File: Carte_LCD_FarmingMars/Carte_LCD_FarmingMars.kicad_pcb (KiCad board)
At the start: 2 copper layers, 17 parts, among them J2 Conn_01x02_Pin, J3 Conn_01x04_Pin, SW1 SW_DIP_x01, SW2 SW_Push, SW3 SW_Push, U1 3V3 reg, U2 ATtiny1616-S

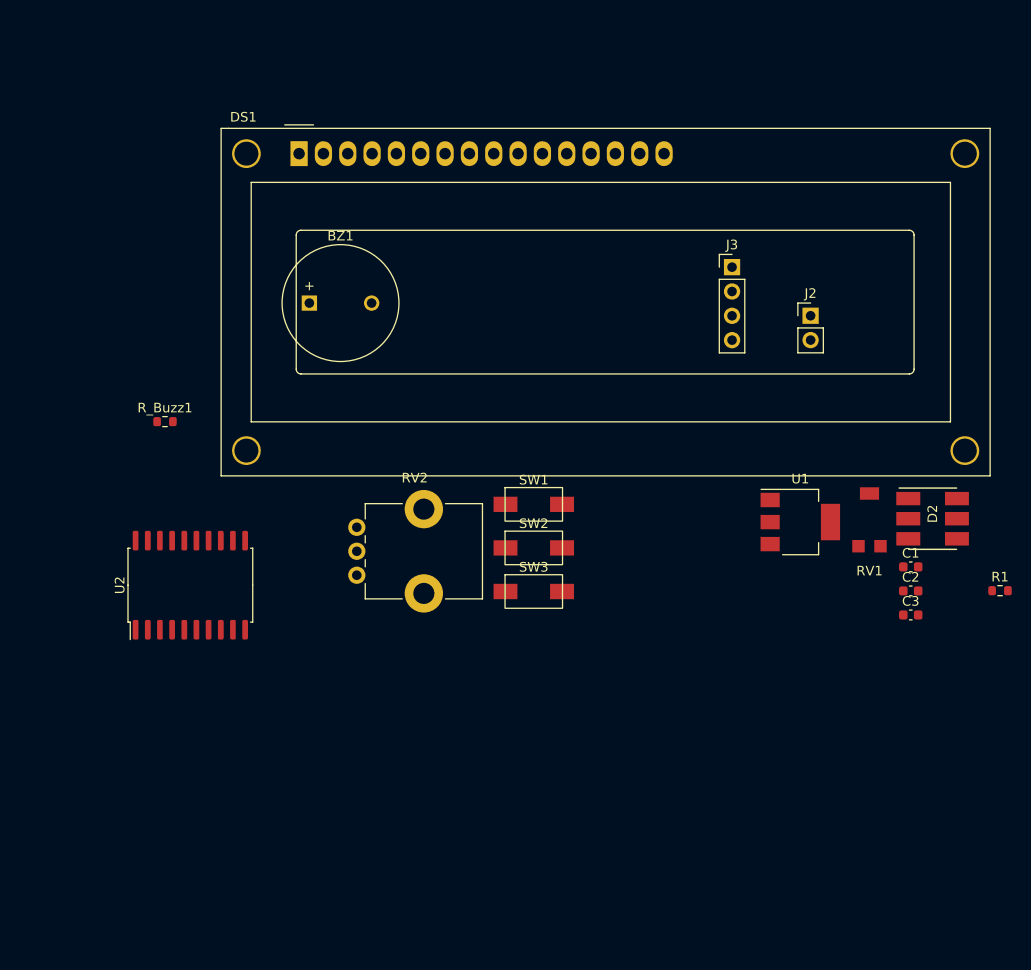
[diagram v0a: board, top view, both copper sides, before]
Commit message: Placement préliminaire PCB
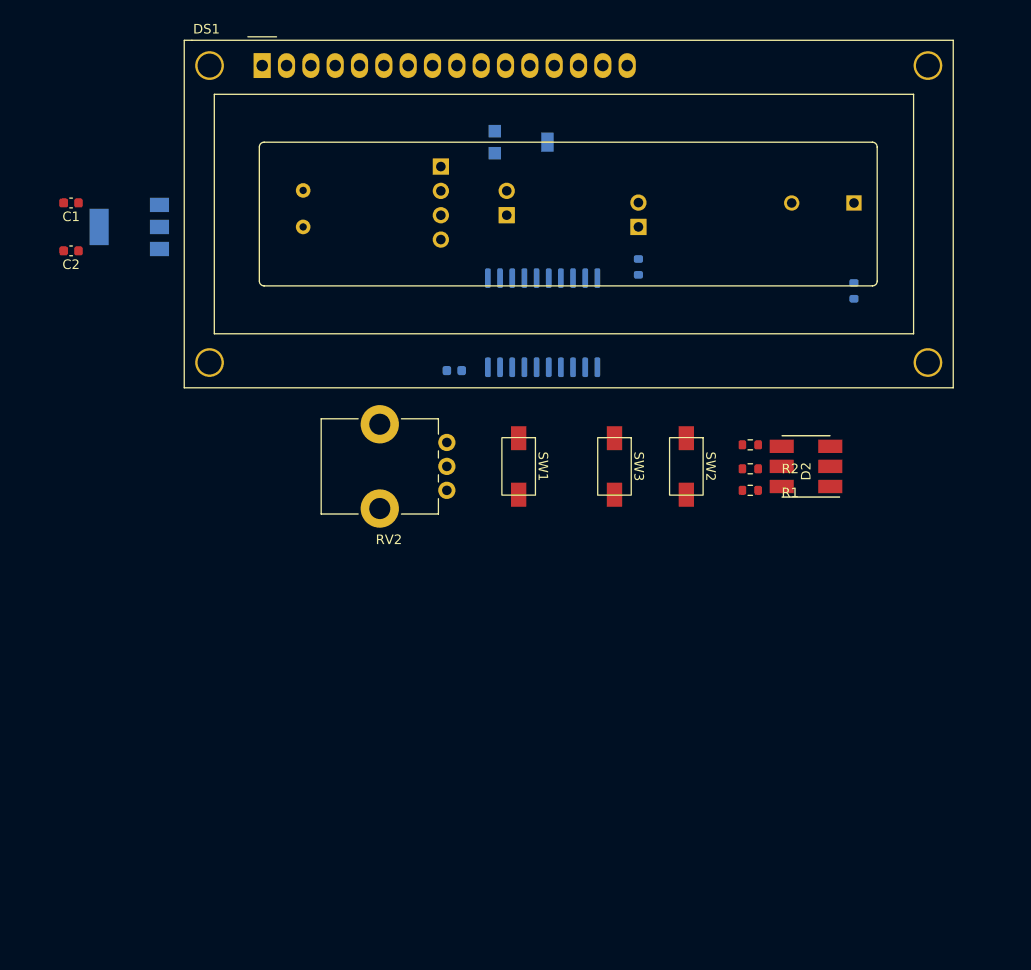
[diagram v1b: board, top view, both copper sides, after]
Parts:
- added J1: Screw_Terminal_01x02, ENAC_robotique:Bornier_2x3.81mm, B.Cu at (107.5, 58.7)
- added J4: Conn_01x02_Pin, Connector_PinHeader_2.54mm:PinHeader_1x02_P2.54mm_Horizontal, B.Cu at (142.5, 62.5)
- added R2: 470, Resistor_SMD:R_0603_1608Metric, F.Cu at (154.2, 87.8)
- added R3: 470, Resistor_SMD:R_0603_1608Metric, F.Cu at (154.2, 85.2)
- added R4: 470, Resistor_SMD:R_0603_1608Metric, B.Cu at (142.5, 66.7)
- BZ1, C3, RV1, R_Buzz1, U1, U2: moved to B.Cu
- J2: footprint Connector_PinHeader_2.54mm:PinHeader_1x02_P2.54mm_Vertical -> Connector_PinHeader_2.54mm:PinHeader_1x02_P2.54mm_Horizontal; moved to B.Cu
- J3: footprint Connector_PinHeader_2.54mm:PinHeader_1x04_P2.54mm_Vertical -> Connector_PinHeader_2.54mm:PinHeader_1x04_P2.54mm_Horizontal; moved to B.Cu
- R1: value 58 -> 470
- moved C1 95.5 mm to (83.3, 60.0), turned to 180 degrees
- moved C2 94.6 mm to (83.3, 65.0), turned to 180 degrees
- moved U1 76.5 mm to (89.3, 62.5), turned to 180 degrees
- moved R_Buzz1 73.2 mm to (165.0, 69.2), turned to 90 degrees
- moved BZ1 57.8 mm to (165.0, 60.0), turned to 180 degrees
- moved C3 54.1 mm to (123.3, 77.5)
- moved RV1 54.0 mm to (130.0, 53.6), turned to 90 degrees
- moved U2 45.9 mm to (132.5, 72.5)
- moved J2 33.4 mm to (128.8, 61.3)
- moved J3 32.2 mm to (121.9, 56.2), turned to 180 degrees
- moved R1 28.1 mm to (154.2, 90.0)
- moved SW2 18.1 mm to (147.5, 87.5), turned to -90 degrees
- moved RV2 16.7 mm to (122.5, 85.0), turned to 180 degrees
- moved SW3 15.5 mm to (140.0, 87.5), turned to -90 degrees
- moved D2 14.3 mm to (160.0, 87.5), turned to 180 degrees
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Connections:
- net +BATT renamed ALIM 5V
- D2 pad 4: BLUE -> Net-(D2-BA)
- D2 pad 5: GREEN -> Net-(D2-GA)
- RV1 pad 1: +5V -> GND
- RV1 pad 3: GND -> +5V
- RV2 pad 1: +5V -> GND
- RV2 pad 3: GND -> +3.3V
- U2 pad 16: unconnected-(U2-~{RESET}/PA0-Pad16) -> Net-(U2-~{RESET}/PA0)

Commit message: placement composants
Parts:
- removed J1: Screw_Terminal_01x02, ENAC_robotique:Bornier_2x3.81mm
- C1, C2: moved to B.Cu
- moved J3 73.5 mm to (88.9, 121.9)
- moved SW2 62.9 mm to (98.4, 126.8)
- moved J4 61.5 mm to (88.9, 92.7), turned to 180 degrees
- moved C2 59.3 mm to (115.2, 114.9), turned to -90 degrees
- moved C1 58.8 mm to (104.1, 114.9), turned to -90 degrees
- moved J2 57.6 mm to (88.9, 102.9), turned to 180 degrees
- moved U1 56.7 mm to (109.5, 115.5), turned to -90 degrees
- moved R_Buzz1 53.3 mm to (127.6, 107.1)
- moved BZ1 50.9 mm to (133.9, 100.3), turned to 0 degrees
- moved SW3 49.1 mm to (110.7, 126.9)
- moved RV1 47.4 mm to (97.9, 88.5), turned to -90 degrees
- moved DS1 40.3 mm to (89.8, 83.6)
- moved SW1 39.9 mm to (122.9, 126.8)
- moved D2 39.7 mm to (156.2, 127.0), turned to 90 degrees
- moved RV2 37.7 mm to (135.4, 120.5), turned to -90 degrees
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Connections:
- C1 pad 1: ALIM 5V -> +5V
- U1 pad 1: ALIM 5V -> +5V
- U2 pad 12: D7 -> D4
- U2 pad 13: D6 -> D5
- U2 pad 14: D5 -> D6
- U2 pad 15: D4 -> D7
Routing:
- net +3.3V: track 0.00 -> 11.6 mm
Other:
- board outline added: 85 x 60 mm

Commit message: Routage, inversion pin Couleur et Vbuzz
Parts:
- moved C3 4.66 mm to (122.6, 102.2)
- moved D2 1.54 mm to (156.2, 128.5)
- moved R2 1.54 mm to (156.2, 120.9)
- moved R1 1.54 mm to (154.3, 120.9)
- moved R3 1.54 mm to (158.3, 120.9)
- moved U2 1.37 mm to (110.1, 98.8)
- moved U1 0.81 mm to (109.5, 116.4)
- moved C2 0.50 mm to (115.2, 115.4)
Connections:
- U2 pad 4: COULEUR -> VBUZZ
- U2 pad 5: VBUZZ -> COULEUR
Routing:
- net RED: track 0.00 -> 85.9 mm, vias 0 -> 3
- net +5V: track 0.00 -> 69.4 mm, vias 0 -> 3
- net GREEN: track 0.00 -> 65.6 mm, vias 0 -> 1
- net BLUE: track 0.00 -> 57.1 mm, vias 0 -> 1
- net +3.3V: track 11.6 -> 58.3 mm, vias 0 -> 4
- net UPDI: track 0.00 -> 40.2 mm
- net UART_Rx: track 0.00 -> 39.0 mm, vias 0 -> 1
- net POTAR: track 0.00 -> 37.7 mm, vias 0 -> 1
- net UART_Tx: track 0.00 -> 35.4 mm, vias 0 -> 1
- net B_OUT: track 0.00 -> 34.5 mm, vias 0 -> 1
- net RS: track 0.00 -> 34.0 mm, vias 0 -> 2
- net COULEUR: track 0.00 -> 29.4 mm, vias 0 -> 1
- net B_IN: track 0.00 -> 26.4 mm, vias 0 -> 1
- net VBUZZ: track 0.00 -> 20.2 mm
- net D7: track 0.00 -> 19.4 mm
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- added copper zone on B.Cu, net GND
- added copper zone on F.Cu, net GND

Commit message: Corrections, Verification , prêt à commander !
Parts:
- added G***: LOGO, ENAC_robotique:logo_enac_moyen, B.Cu at (151.0, 93.6)
- renumbered U2 to ATTINY, BZ1 to BUZZER, C1 to C100n, C3 to C100n, C2 to C10u, SW2 to COLOR, SW1 to OK, R_Buzz1 to R330, R1 to R470, R4 to R470, U1 to REGU, SW3 to RETURN, D2 to RGB, RV2 to SELECT, J2 to TIRETTE, J3 to UART, J4 to UPDI
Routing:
- net +5V: track 69.4 -> 93.7 mm, vias 3 -> 4
- net RED: track 85.9 -> 74.5 mm
- net GREEN: track 65.6 -> 60.4 mm
- net RS: track 34.0 -> 29.7 mm, vias 2 -> 1
- net BLUE: track 57.1 -> 53.6 mm
- net E: track 18.1 -> 15.0 mm
- net POTAR: track 37.7 -> 34.8 mm
- net UART_Rx: track 39.0 -> 36.2 mm, vias 1 -> 0
- net Net-(BZ1--): track 11.8 -> 9.34 mm, vias 1 -> 0
- net B_OUT: track 34.5 -> 32.2 mm
- net +3.3V: track 58.3 -> 56.2 mm, vias 4 -> 2
- net D4: track 17.7 -> 15.9 mm
- net D5: track 18.4 -> 16.7 mm
- net UART_Tx: track 35.4 -> 34.1 mm, vias 1 -> 0
- net D6: track 18.7 -> 17.4 mm
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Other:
- board text added: "GND"
- board text added: "INTERFACE 2024 BY TIANUI@ENAC"

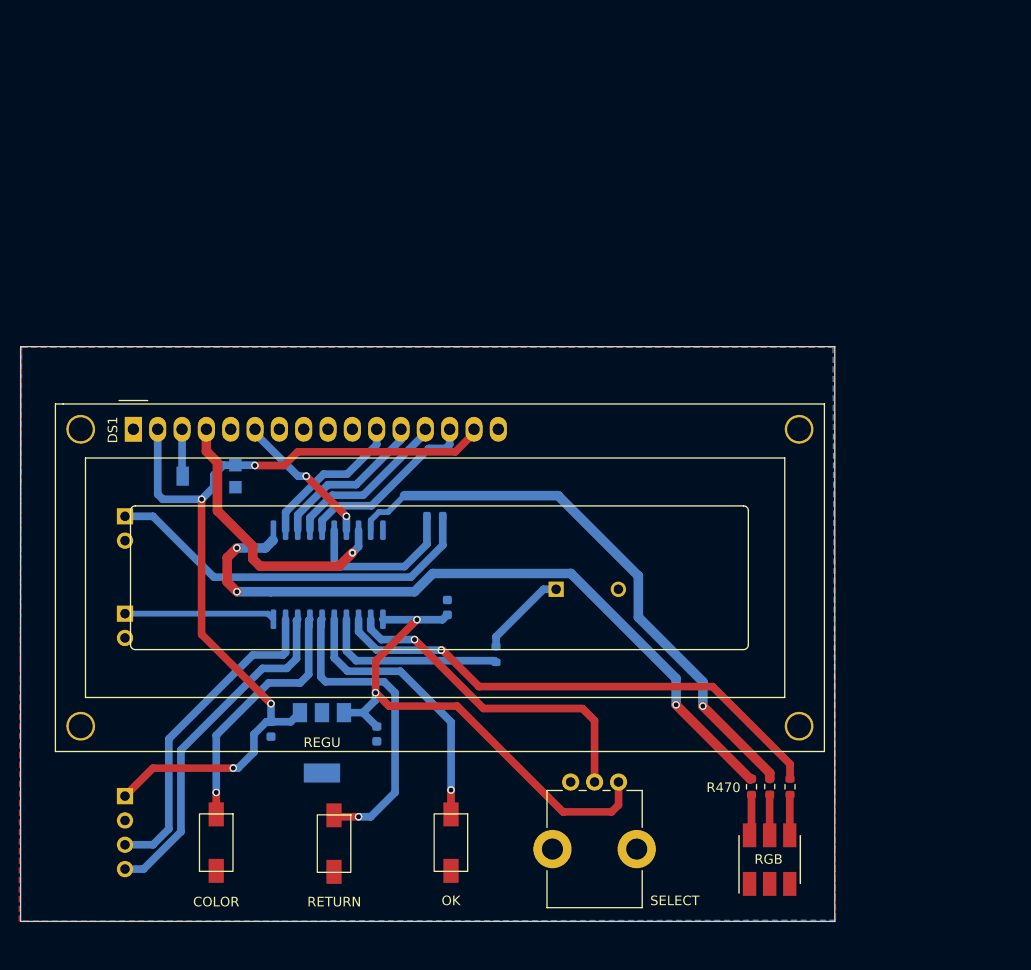
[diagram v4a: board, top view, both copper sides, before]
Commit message: trou + bug footprints
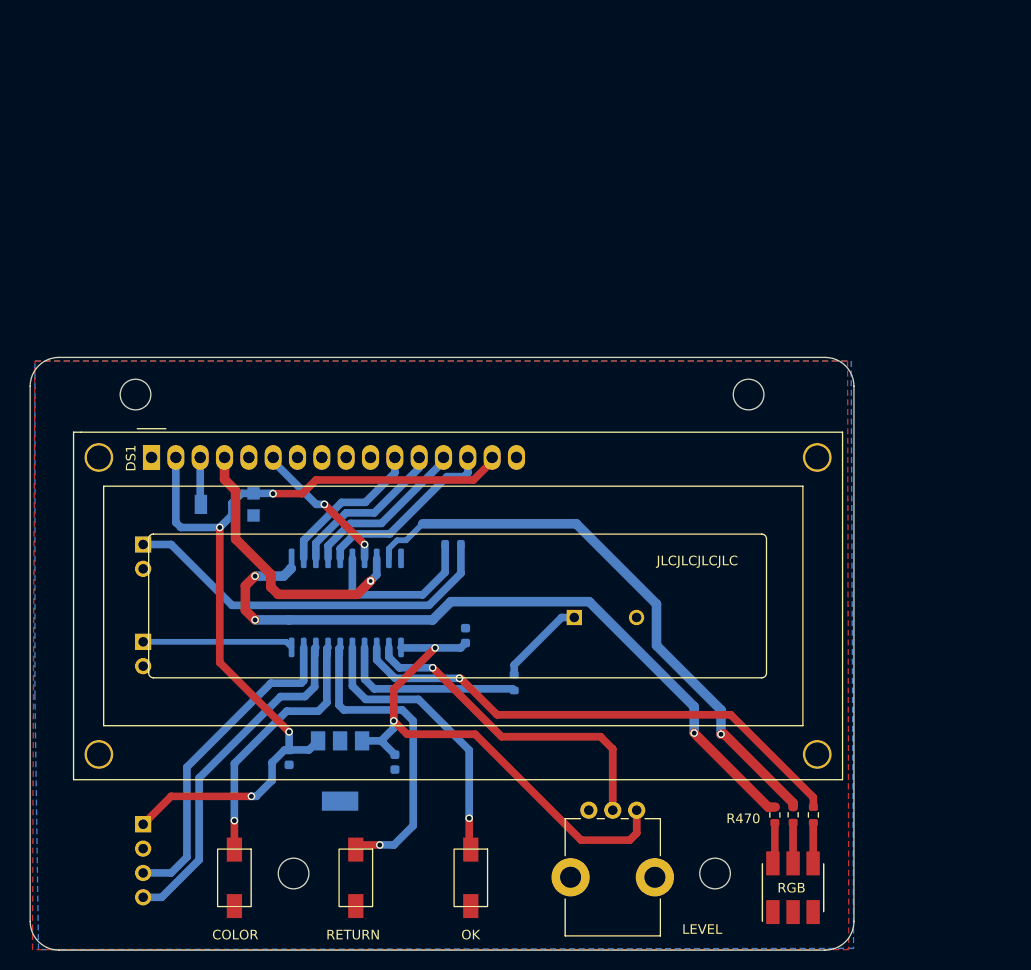
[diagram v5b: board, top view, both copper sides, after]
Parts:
- removed COLOR: SW_Push, ENAC_robotique:SWITCH_DTSM31NV
- removed OK: SW_DIP_x01, ENAC_robotique:SWITCH_DTSM31NV
- added H1: MountingHole, MountingHole:MountingHole_3.2mm_M3, F.Cu at (90.0, 80.0)
- added H2: MountingHole, MountingHole:MountingHole_3.2mm_M3, F.Cu at (154.0, 80.0)
- added H3: MountingHole, MountingHole:MountingHole_3.2mm_M3, F.Cu at (106.5, 130.0)
- added H4: MountingHole, MountingHole:MountingHole_3.2mm_M3, F.Cu at (150.5, 130.0)
- added SW1: SW_DIP_x01, ENAC_robotique:SWITCH_DTSM31NV, F.Cu at (125.0, 130.4)
- added SW2: SW_Push, ENAC_robotique:SWITCH_DTSM31NV, F.Cu at (100.3, 130.4)
- moved SW3 4.24 mm to (113.0, 130.4)
- moved R1 3.82 mm to (156.7, 123.9)
- moved R2 3.82 mm to (158.7, 123.9)
- moved R3 3.82 mm to (160.8, 123.9)
- moved D2 3.82 mm to (158.6, 131.5)
- moved C3 3.50 mm to (124.5, 105.2)
- moved J4 3.50 mm to (90.8, 95.7)
- moved BZ1 3.50 mm to (135.8, 103.3)
- moved C2 3.50 mm to (117.1, 118.4)
- moved G*** 3.50 mm to (152.9, 96.5)
- moved U1 3.50 mm to (111.4, 119.3)
- moved U2 3.50 mm to (112.0, 101.7)
- moved C1 3.50 mm to (106.0, 117.9)
- moved DS1 3.50 mm to (91.7, 86.6)
- moved J2 3.50 mm to (90.8, 105.8)
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- renumbered BUZZER to BZ1, C100n to C1, C10u to C2, C100n to C3, RGB to D2, TIRETTE to J2, UART to J3, UPDI to J4, R470 to R1, R470 to R4, SELECT to RV2, R330 to R_Buzz1, RETURN to SW3, REGU to U1, ATTINY to U2
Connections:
- U2 pad 5: COULEUR -> B_IN
- U2 pad 7: B_IN -> COULEUR
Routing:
- net B_IN: track 26.4 -> 29.4 mm
- net COULEUR: track 28.6 -> 27.1 mm
- net RED: track 74.5 -> 75.1 mm
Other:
- board size 85 x 60 mm -> 86 x 61.9 mm
- board text added: "+"
- board text added: "-"
- board text added: "ATTINY"
- board text added: "C100n"
- board text added: "C10u"
- board text added: "COLOR"
- board text added: "JLCJLCJLCJLC"
- board text added: "LEVEL"
- board text added: "OK"
- board text added: "R330"
- board text added: "R470"
- board text added: "REGU"
- board text added: "RETURN"
- board text added: "RGB"
- board text added: "RX"
- board text added: "TIRETTE"
- board text added: "TX"
- board text added: "UART"
- board text added: "UPDI"
